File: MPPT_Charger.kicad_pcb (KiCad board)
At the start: 2 copper layers, 86.8 x 60.8 mm, 117 parts, among them J1 Solar, J2 Battery, J3 USB_B_Mini, J4 INTERFACE PORT, J6 JTAG, J8 Micro_SD_Card_Det_Hirose_DM3AT, J9 IIC RTC, Q1 CSD19505KCS, Q11 CSD19505KCS, Q12 CSD19505KCS, Q13 CSD19505KCS, Q2 CSD19505KCS, Q3 CSD19505KCS, Q4 Si2306, Q5 MMBT3904 1A, Q6 MMBT3904 1A, Q7 Si2306, U1 ACS712, U10 ADS1015, U2 B1212S, U3 AMS1117-5.0, U4 AMS1117-3.3, U5 XL7005A, U6 XL7005A, U7 IR2104, U8 ESP32, U9 CH340G

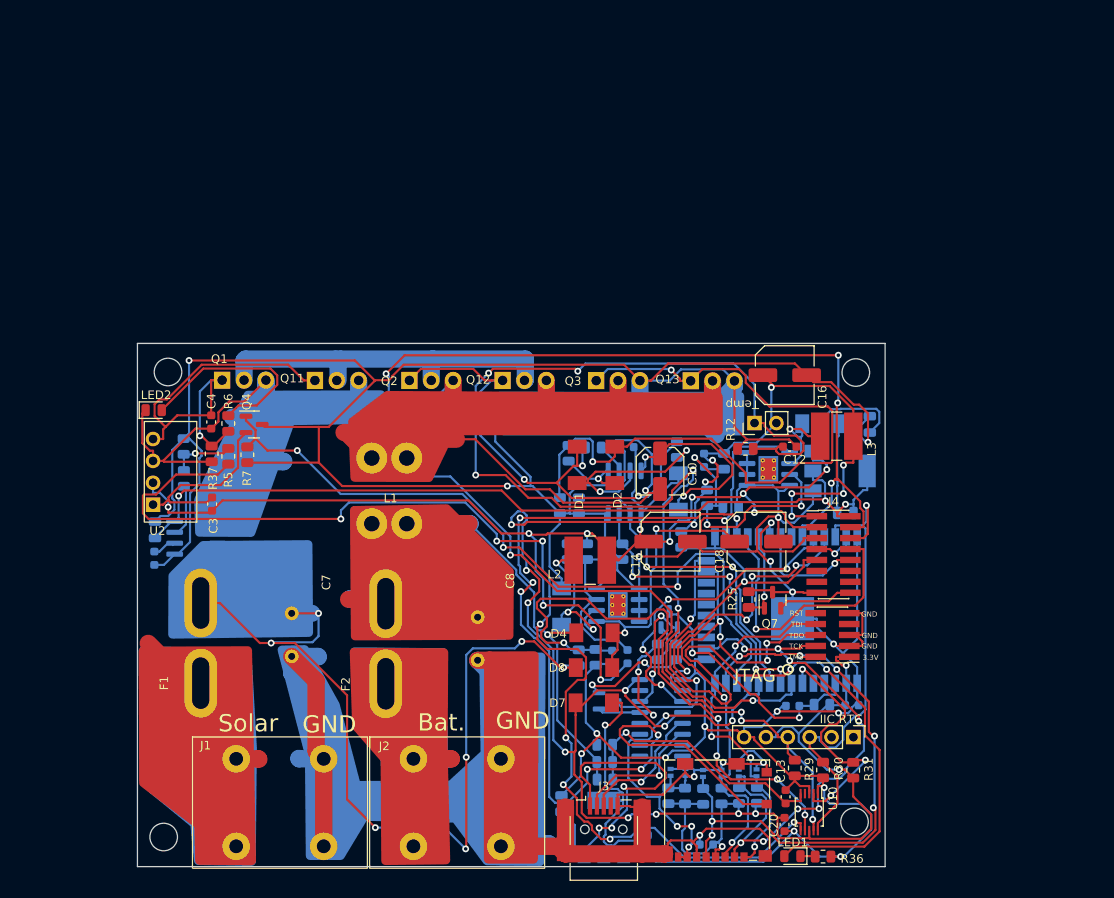
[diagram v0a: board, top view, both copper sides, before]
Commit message: Heatsink and insulation ToDo: Smaller heatsink
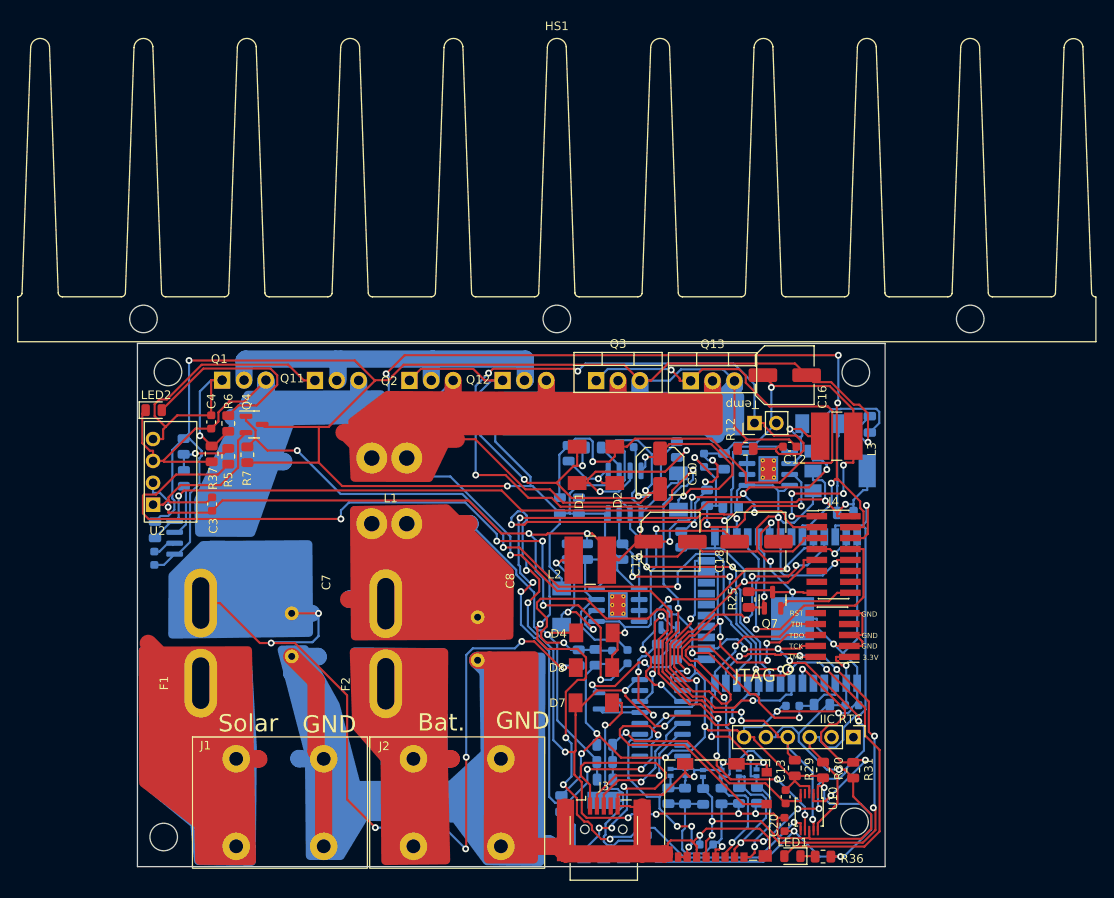
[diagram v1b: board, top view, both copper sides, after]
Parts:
- added HS1: Heatsink_Pad, Heatsink:Heatsink_125x35x50mm_3xFixationM3, F.Cu at (127.2, 91.3)
- Q13, Q3: footprint Package_TO_SOT_THT:TO-220-3_Vertical -> Library:TO-220-3_Vertical_Insulated

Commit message: Heat sink size corrected
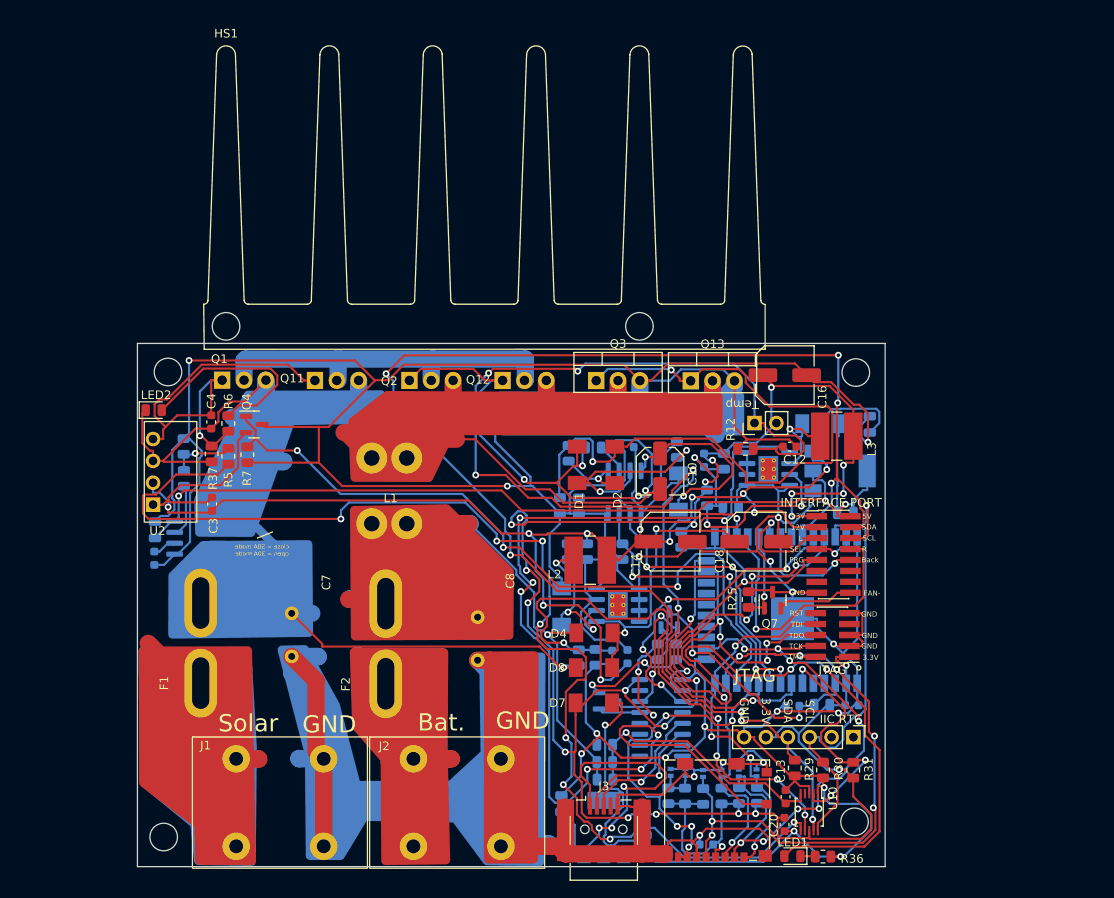
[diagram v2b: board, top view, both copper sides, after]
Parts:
- moved HS1 38.4 mm to (88.7, 92.2)
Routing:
- net Net-(C7-Pad1): track 121.4 -> 60.8 mm, vias 7 -> 1
- net Net-(C10-Pad2): track 127.5 -> 112.2 mm
- net SDA: track 184.6 -> 174.7 mm
- net (no net): track 0.00 -> 2.72 mm
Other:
- board text added: "close = 50A mode open = 30A mode"

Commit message: Footprint C+R changed to 0603 where possible
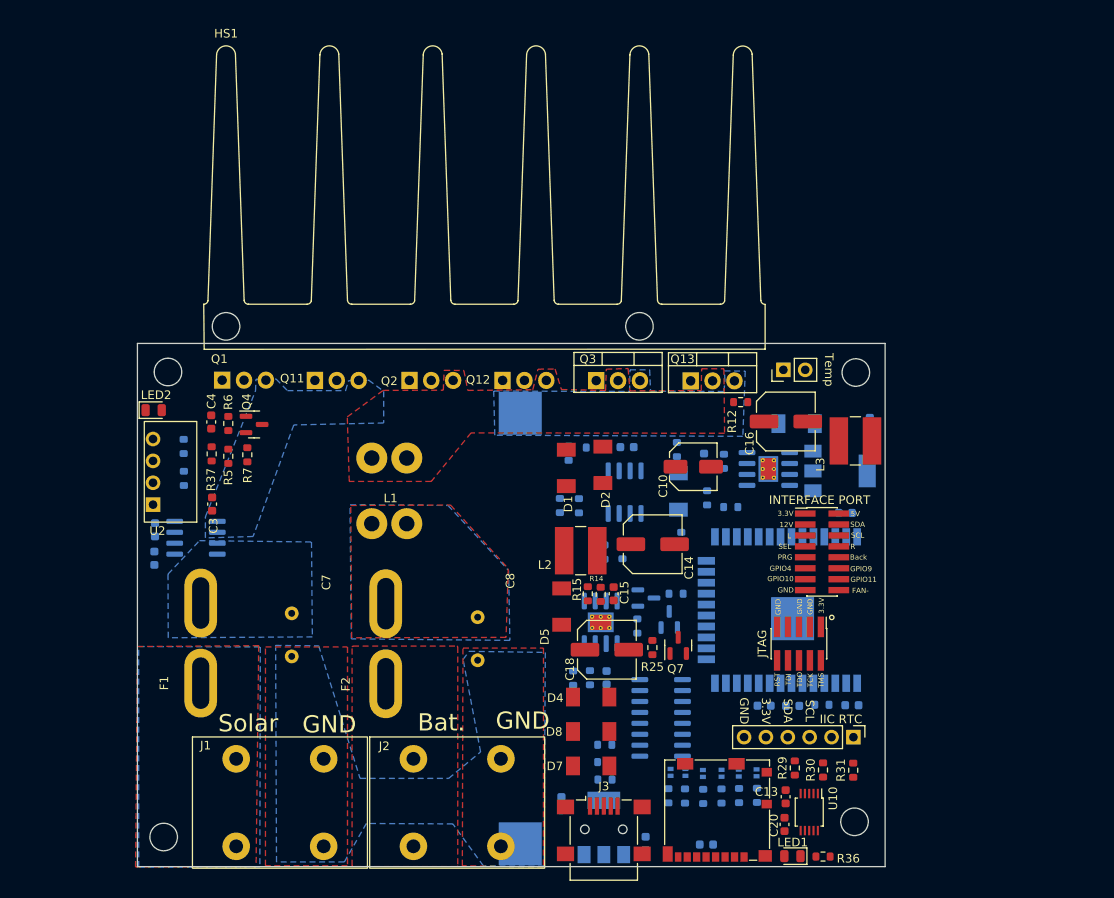
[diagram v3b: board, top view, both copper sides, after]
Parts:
- C12: moved to B.Cu
- C15, D5: moved to F.Cu
- C21, C22, C5, C6, C9: footprint Capacitor_SMD:C_0805_2012Metric -> Capacitor_SMD:C_0603_1608Metric
- R1, R10, R11, R12, R13, R16, R17, R18, R19, R2, R20, R21, R22, R23, R24, R25, R26, R27, R28, R29, R3, R30, R31, R32, R33, R34, R36, R37, R38, R39, R4, R40, R5, R6, R7, R8, R9: footprint Resistor_SMD:R_0805_2012Metric -> Resistor_SMD:R_0603_1608Metric
- R14, R15: footprint Resistor_SMD:R_0805_2012Metric -> Resistor_SMD:R_0603_1608Metric; moved to F.Cu
- moved C12 30.2 mm to (151.2, 136.2), turned to 180 degrees
- moved C18 21.4 mm to (133.0, 129.8)
- moved Q6 12.8 mm to (137.5, 123.8)
- moved R25 12.5 mm to (138.2, 129.5)
- moved Q7 12.1 mm to (141.2, 129.2)
- moved C15 7.48 mm to (133.8, 123.2), turned to -90 degrees
- moved D4 7.47 mm to (131.1, 135.2)
- moved D8 7.43 mm to (131.1, 139.2)
- moved D7 7.34 mm to (131.1, 143.2)
- moved R35 7.03 mm to (153.5, 97.2)
- moved R23 6.75 mm to (141.0, 123.2), turned to 180 degrees
- moved R12 5.45 mm to (148.5, 101.0)
- moved R15 5.41 mm to (130.8, 123.2)
- moved C16 5.39 mm to (153.8, 103.2)
- moved R14 5.21 mm to (132.2, 123.3)
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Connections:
- J4 pad 11: unconnected-(J4-Pad11) -> GPIO4
- J4 pad 12: unconnected-(J4-Pad12) -> GPIO9
- J4 pad 13: unconnected-(J4-Pad13) -> GPIO10
- J4 pad 14: unconnected-(J4-Pad14) -> GPIO11
- U8 pad 17: unconnected-(U8-Pad17) -> GPIO9
- U8 pad 18: unconnected-(U8-Pad18) -> GPIO10
- U8 pad 19: unconnected-(U8-Pad19) -> GPIO11
- U8 pad 26: unconnected-(U8-Pad26) -> GPIO4
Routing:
- net GND: track 588.4 -> 0.00 mm, vias 17 -> 0
- net +3.3V: track 250.4 -> 0.00 mm, vias 21 -> 0
- net GND2: track 201.5 -> 0.00 mm, vias 4 -> 0
- net SDA: track 174.7 -> 0.00 mm, vias 8 -> 0
- net +12V: track 170.3 -> 0.00 mm, vias 11 -> 0
- net Net-(C12-Pad1): track 138.2 -> 0.00 mm, vias 6 -> 0
- net A2: track 135.7 -> 0.00 mm, vias 8 -> 0
- net Net-(C8-Pad1): track 132.8 -> 0.00 mm, vias 1 -> 0
- net Net-(C10-Pad2): track 112.2 -> 0.00 mm, vias 1 -> 0
- net SD_DET_B: track 107.7 -> 0.00 mm, vias 7 -> 0
- net +5V: track 100.7 -> 0.00 mm, vias 3 -> 0
- net BCCU: track 85.8 -> 0.00 mm, vias 3 -> 0
- net Net-(LED1-Pad2): track 84.7 -> 0.00 mm, vias 3 -> 0
- net Net-(D2-Pad1): track 83.1 -> 0.00 mm, vias 2 -> 0
- net Net-(C4-Pad2): track 72.0 -> 0.00 mm
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- added copper zone on B.Cu, net GND
- added copper zone on B.Cu, net GND2
- added copper zone on F.Cu, net GND2
- added copper zone on F.Cu, net Net-(C10-Pad2)
- added copper zone on B.Cu, net Net-(C4-Pad2)
- added copper zone on B.Cu, net Net-(C7-Pad1)
- added copper zone on B.Cu, net Net-(C8-Pad1)
- added copper zone on F.Cu, net Net-(C8-Pad1)
- added copper zone on B.Cu, net Net-(F1-Pad1)
- added copper zone on F.Cu, net Net-(F1-Pad1)
- added copper zone on F.Cu, net Net-(F2-Pad1)
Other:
- board text removed: "JTAG"
- board text removed: "close = 50A mode open = 30A mode"

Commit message: Done ?
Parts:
- moved U10 29.9 mm to (148.4, 119.8), turned to 180 degrees
- moved R30 27.2 mm to (156.7, 116.5)
- moved R29 26.9 mm to (154.2, 116.6)
- moved J9 26.9 mm to (160.9, 113.1)
- moved C20 26.4 mm to (148.2, 124.2), turned to 180 degrees
- moved R31 25.0 mm to (148.2, 122.6), turned to 0 degrees
- moved J6 13.7 mm to (159.8, 142.0)
- moved C6 12.7 mm to (163.4, 101.4), turned to 0 degrees
- moved J4 6.80 mm to (156.9, 125.1)
- moved C5 6.20 mm to (157.9, 100.9), turned to 180 degrees
- moved U3 2.97 mm to (160.4, 106.0)
- moved D6 2.46 mm to (152.8, 102.4), turned to -90 degrees
- moved R19 2.44 mm to (145.3, 114.5)
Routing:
- net GND: track 0.00 -> 383.7 mm, vias 0 -> 20
- net +3.3V: track 0.00 -> 199.5 mm, vias 0 -> 4
- net +12V: track 0.00 -> 147.0 mm, vias 0 -> 2
- net +5V: track 0.00 -> 132.1 mm, vias 0 -> 3
- net GND2: track 0.00 -> 87.1 mm, vias 0 -> 7
- net BCCU: track 0.00 -> 76.8 mm, vias 0 -> 3
- net A2: track 0.00 -> 76.4 mm, vias 0 -> 6
- net Net-(C12-Pad1): track 0.00 -> 76.0 mm, vias 0 -> 2
- net Net-(C18-Pad1): track 0.00 -> 66.1 mm, vias 0 -> 2
- net A1: track 0.00 -> 65.7 mm, vias 0 -> 3
- net Net-(LED1-Pad2): track 0.00 -> 57.7 mm, vias 0 -> 1
- net SD_CMD: track 0.00 -> 57.3 mm, vias 0 -> 4
- net SD_DET_B: track 0.00 -> 56.9 mm, vias 0 -> 1
- net SD_DAT3: track 0.00 -> 56.8 mm, vias 0 -> 3
- net Net-(D2-Pad1): track 0.00 -> 54.5 mm, vias 0 -> 1
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
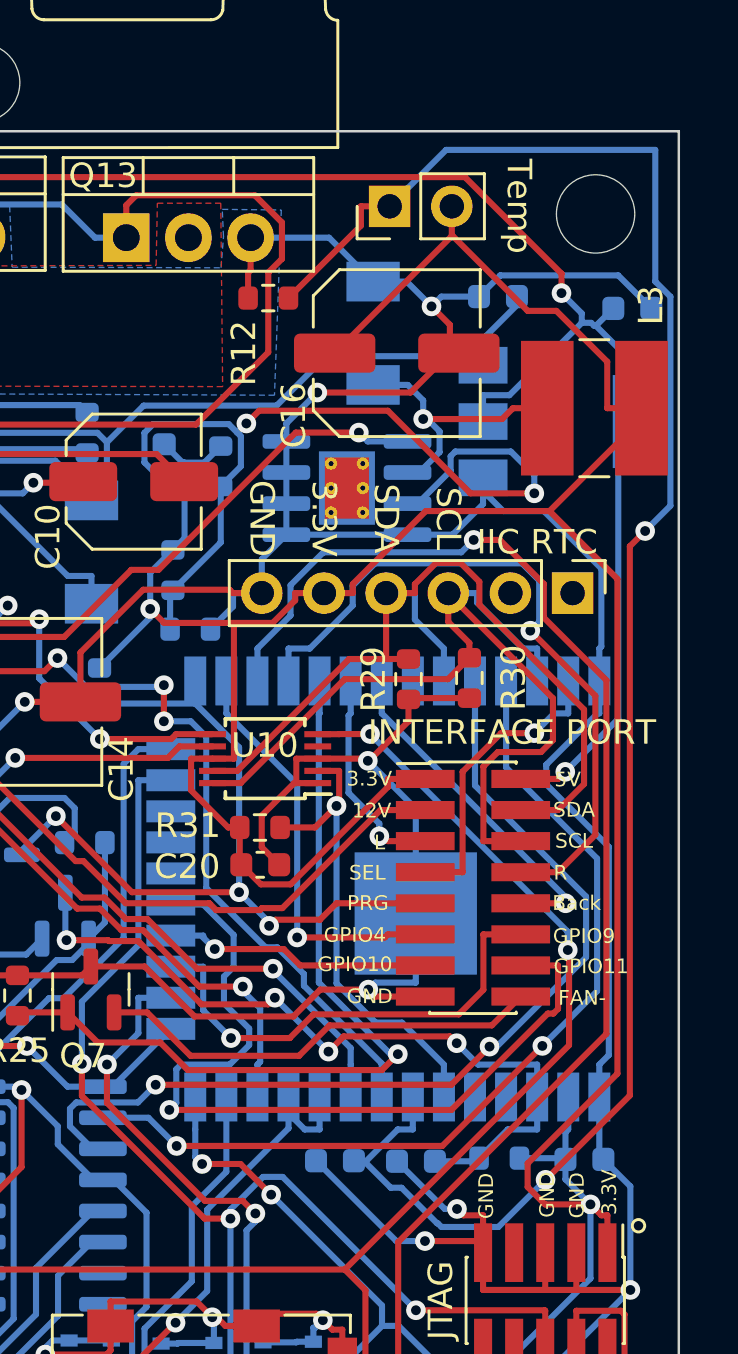
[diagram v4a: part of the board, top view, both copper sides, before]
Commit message: footprint for ADS1115 updated
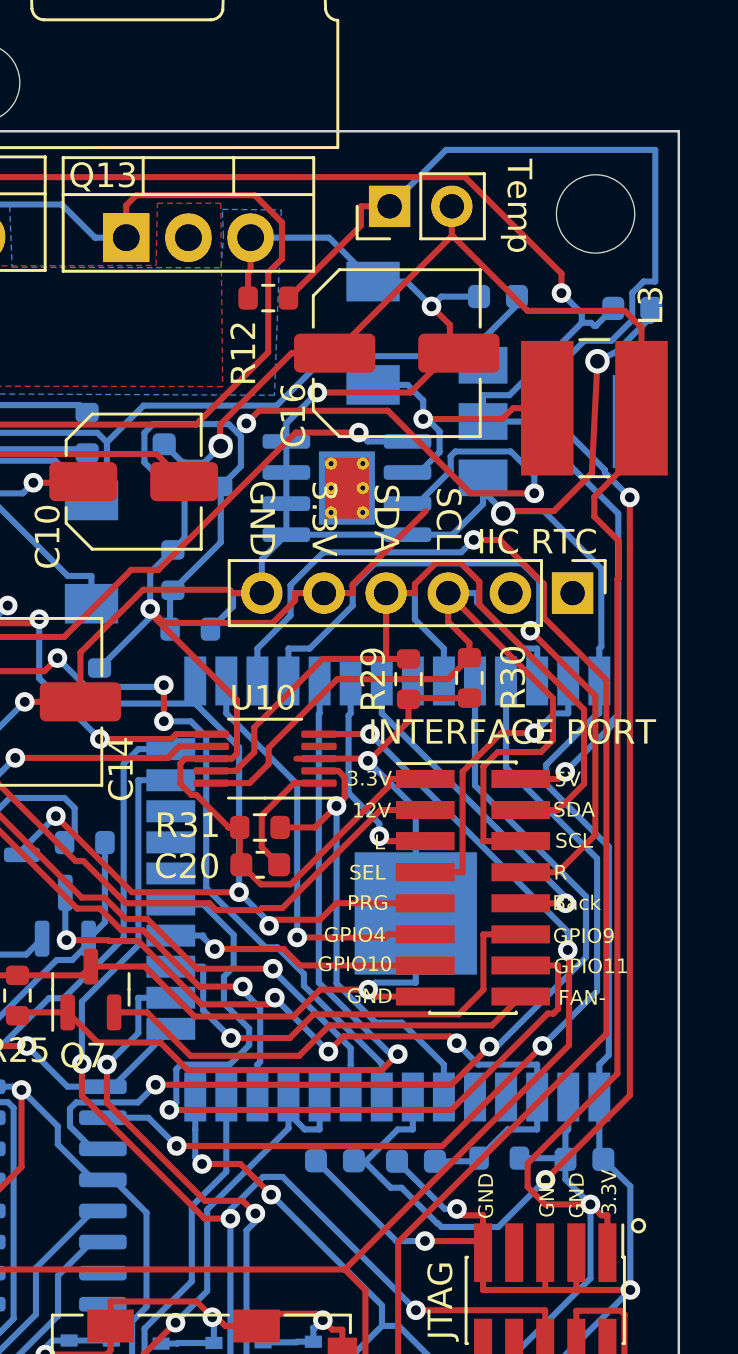
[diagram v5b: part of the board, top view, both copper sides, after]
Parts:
- U10: footprint Package_SO:TSSOP-10_3x3mm_P0.5mm -> Package_SO:VSSOP-10_3x3mm_P0.5mm
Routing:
- net +3.3V: track 199.5 -> 205.8 mm, vias 4 -> 5
- net GND: track 383.7 -> 386.9 mm, vias 20 -> 22
- net Net-(C12-Pad1): track 76.0 -> 79.0 mm
- net SDA: track 35.8 -> 36.4 mm

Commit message: Footprint updates for some parts (mainly too small drill holes for screw terminal and larger capacitors)
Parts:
- C7, C8: footprint Capacitor_THT:C_Radial_D12.5mm_H20.0mm_P5.00mm -> Library:C_Radial_D12.5mm_H20.0mm_P5.00mm
- J1, J2: footprint footprints:TerminalBlock_DEGSON_DG135T -> Library:TerminalBlock_DEGSON_DG135T
- U10: footprint Package_SO:VSSOP-10_3x3mm_P0.5mm -> Package_SO:TSSOP-10_3x3mm_P0.5mm
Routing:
- net +5V: track 131.8 -> 137.3 mm
- net GND: track 386.9 -> 388.2 mm

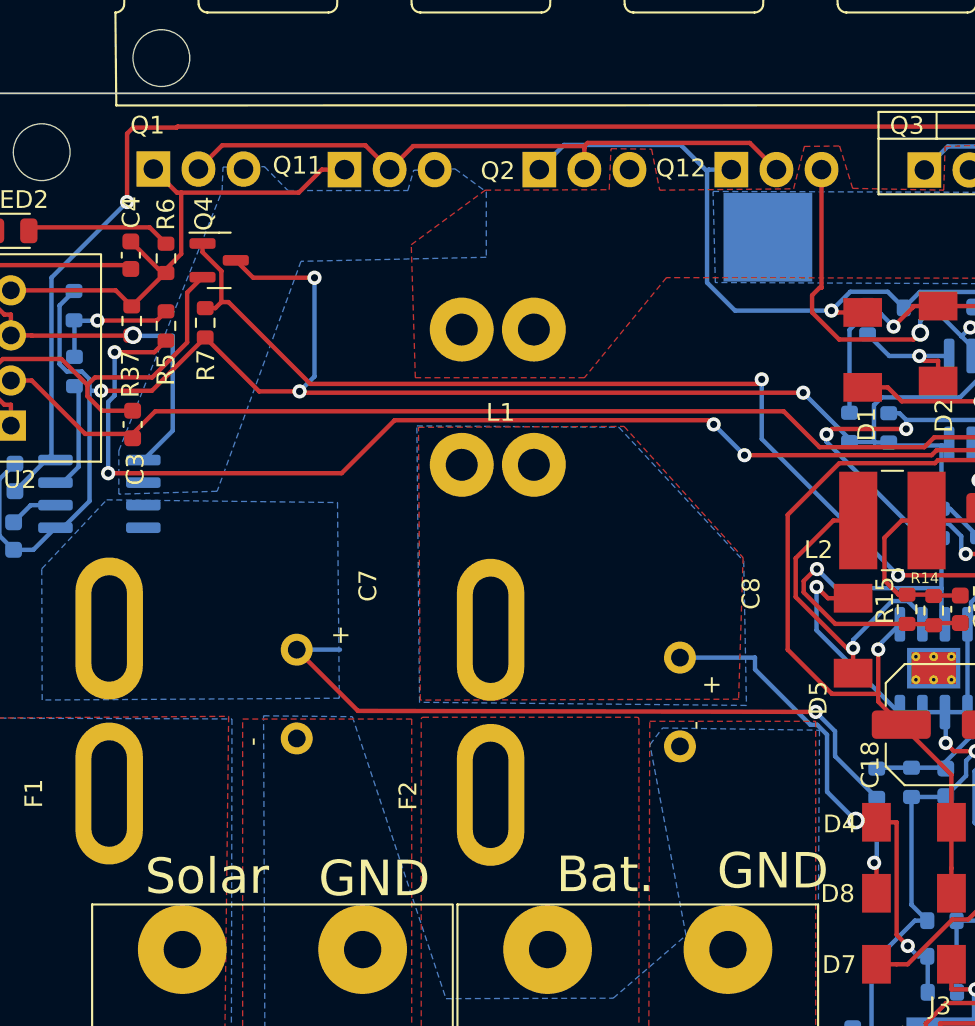
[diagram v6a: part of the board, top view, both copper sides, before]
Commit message: Footprint for 470uF was too small Some more minor changes
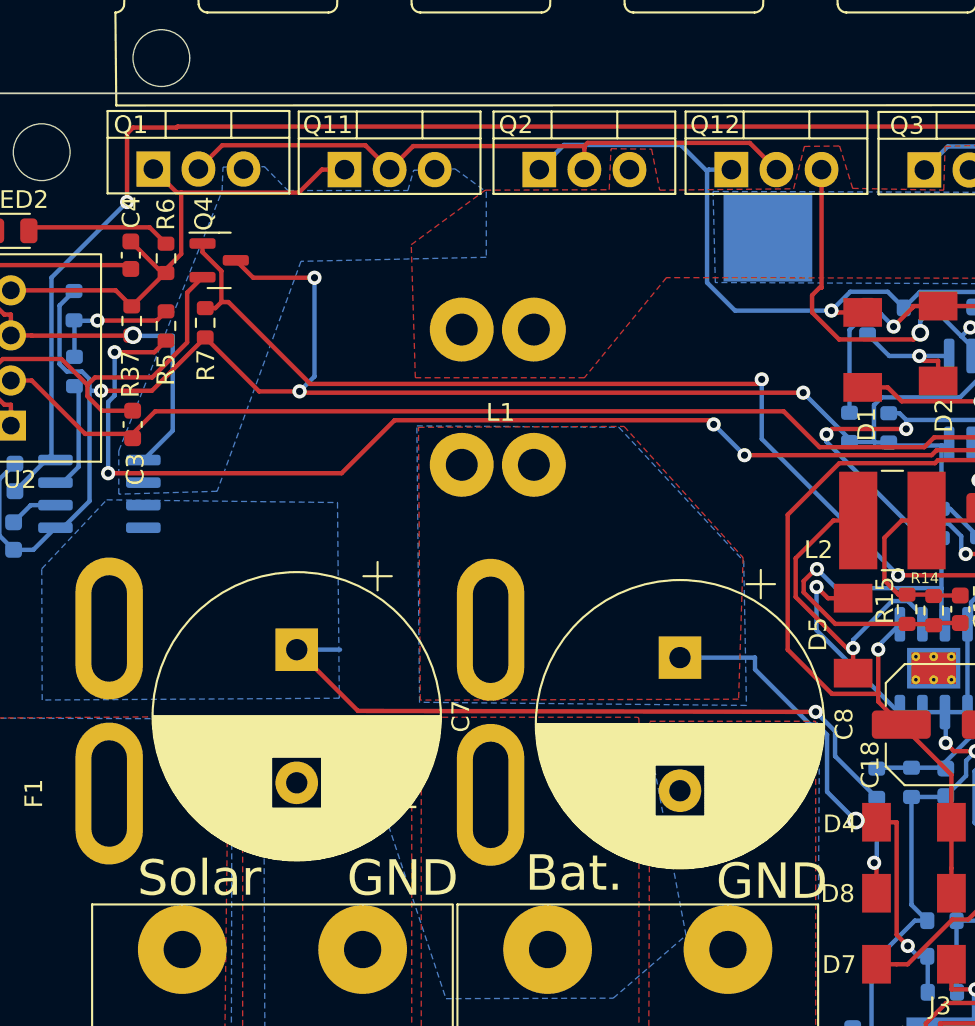
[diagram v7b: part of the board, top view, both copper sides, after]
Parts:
- C7, C8: footprint Library:C_Radial_D12.5mm_H20.0mm_P5.00mm -> Capacitor_THT:CP_Radial_D16.0mm_P7.50mm
